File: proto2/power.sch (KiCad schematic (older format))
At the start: 2 parts, among them U13 AP1117-50, U14 JTD1548S15

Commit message: Routed Board.
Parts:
- removed U14: JTD1548S15, Converter_DCDC:Converter_DCDC_XP_POWER_JTDxxxxxxx_THT, symbol Converter_DCDC:JTD1548S15
- added C43, C49: 1nF 2kV, Capacitor_SMD:C_0805_2012Metric, symbol Device:C_Small
- added C44, C47: 330uF, Capacitor_SMD:C_0805_2012Metric, symbol Device:CP1_Small
- added C45, C46: 4.7uF, Capacitor_SMD:C_0805_2012Metric, symbol Device:C_Small
- added C48: 100uF, Capacitor_SMD:C_0805_2012Metric, symbol Device:C_Small
- added C50: 0.33uF, Capacitor_SMD:C_0805_2012Metric, symbol Device:C_Small
- added C51: 01.uF, Capacitor_SMD:C_0805_2012Metric, symbol Device:C_Small
- added C52, C53: 0.1uF, Capacitor_SMD:C_1206_3216Metric, symbol Device:C_Small
- added F13: 1A, Resistor_SMD:R_1206_3216Metric, symbol Device:Polyfuse_Small
- added F14, F15, F16, F17: 500mA, Resistor_SMD:R_0805_2012Metric, symbol Device:Polyfuse_Small
- added L43: 2.2uH, Inductor_BCR:Murata_LQH32PN2R2NN0L, symbol Device:L_Core_Ferrite_Small
- added PS1: CUI PDQE20, Converter_BCR:CUI_PDQE20, symbol BCR:CUI_PDQE20_ISOLATED_DCDC
- added R17, R18: 0R, Resistor_SMD:R_0805_2012Metric, symbol Device:R_Small
- added R19: R Trim Up, Capacitor_SMD:C_0805_2012Metric, symbol Device:R_Small
- added R20: R Trim Down, Capacitor_SMD:C_0805_2012Metric, symbol Device:R_Small
- added R21: 0R, Capacitor_SMD:C_1206_3216Metric, symbol Device:R_Small
- U13: value AP1117-50 -> LDO
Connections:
- net labels added: 5V_1, 5V_2, 5V_3, 5V_4, GNDPWR, TRIM, VIN
- wire segments 15 -> 93
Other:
- note added: "DNP:\nC50\nC51\nU13"
- note added: "DNP:\nC52\nC53\nR18"
- note added: "DNP:\nR19\nR20"
- note added: "https://electronics.stackexchange.com/questions/19561/should-chassis-ground-be-attached-to-digital-ground"
- moved on the sheet: U13

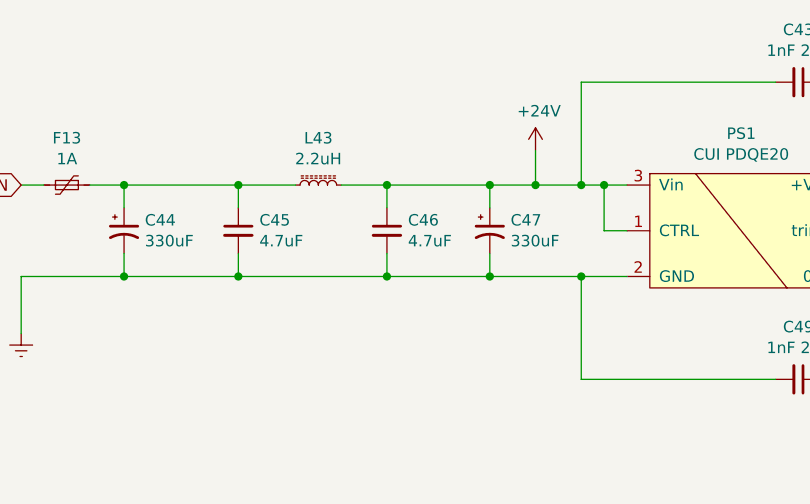
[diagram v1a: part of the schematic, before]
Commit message: Added correct cap and moved DIP switches.
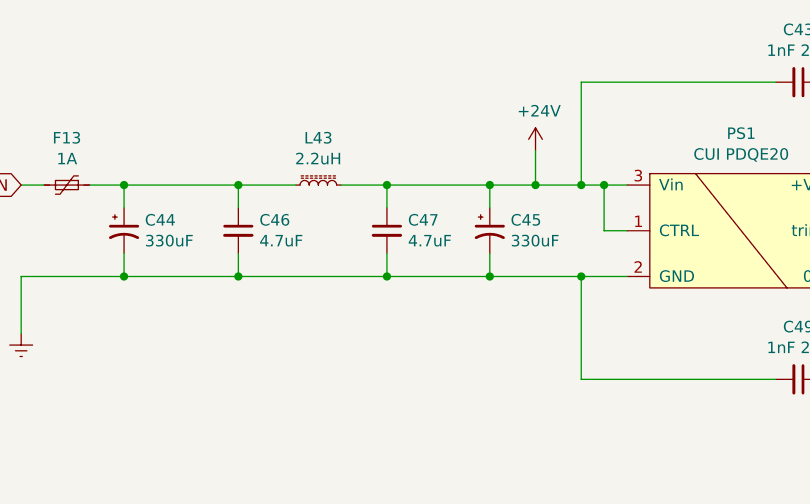
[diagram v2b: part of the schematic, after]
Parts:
- C44: footprint Capacitor_SMD:C_0805_2012Metric -> Capacitor_BCR:CP_Elec_13x12.5
- C45: renamed from C47; footprint Capacitor_SMD:C_0805_2012Metric -> Capacitor_BCR:CP_Elec_13x12.5
- U13: footprint Package_TO_SOT_SMD:SOT-223-3_TabPin2 -> JLCPCB:TO-252-2
- renumbered C45 to C46, C46 to C47
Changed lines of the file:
@@
 F 0 "U13" H 3900 5742 50  0000 C CNN
 F 1 "LDO" H 3900 5651 50  0000 C CNN
-F 2 "Package_TO_SOT_SMD:SOT-223-3_TabPin2" H 3900 5700 50  0001 C CNN
+F 2 "JLCPCB:TO-252-2" H 3900 5700 50  0001 C CNN
 F 3 "http://www.diodes.com/datasheets/AP1117.pdf" H 4000 5250 50  0001 C CNN
 	1    3900 5500
@@
 F 0 "C44" H 1441 2046 50  0000 L CNN
 F 1 "330uF" H 1441 1955 50  0000 L CNN
-F 2 "Capacitor_SMD:C_0805_2012Metric" H 1350 2000 50  0001 C CNN
+F 2 "Capacitor_BCR:CP_Elec_13x12.5" H 1350 2000 50  0001 C CNN
 F 3 "~" H 1350 2000 50  0001 C CNN
 	1    1350 2000
@@
 $EndComp
 $Comp
-L Device:CP1_Small C47
+L Device:CP1_Small C45
 U 1 1 61BAC8B9
 P 2950 2000
-F 0 "C47" H 3041 2046 50  0000 L CNN
+F 0 "C45" H 3041 2046 50  0000 L CNN
 F 1 "330uF" H 3041 1955 50  0000 L CNN
-F 2 "Capacitor_SMD:C_0805_2012Metric" H 2950 2000 50  0001 C CNN
+F 2 "Capacitor_BCR:CP_Elec_13x12.5" H 2950 2000 50  0001 C CNN
 F 3 "~" H 2950 2000 50  0001 C CNN
 	1    2950 2000
@@
 $EndComp
 $Comp
-L Device:C_Small C46
+L Device:C_Small C47
 U 1 1 61BB6AD1
 P 2500 2000
-F 0 "C46" H 2592 2046 50  0000 L CNN
+F 0 "C47" H 2592 2046 50  0000 L CNN
 F 1 "4.7uF" H 2592 1955 50  0000 L CNN
 F 2 "Capacitor_SMD:C_0805_2012Metric" H 2500 2000 50  0001 C CNN
@@
 $EndComp
 $Comp
-L Device:C_Small C45
+L Device:C_Small C46
 U 1 1 61BB959C
 P 1850 2000
-F 0 "C45" H 1942 2046 50  0000 L CNN
+F 0 "C46" H 1942 2046 50  0000 L CNN
 F 1 "4.7uF" H 1942 1955 50  0000 L CNN
 F 2 "Capacitor_SMD:C_0805_2012Metric" H 1850 2000 50  0001 C CNN

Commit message: Finished routing board and other changes, bad commit message, I know.
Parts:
- C43, C49: footprint Capacitor_SMD:C_0805_2012Metric -> Capacitor_SMD:C_1206_3216Metric; LCSC (none) -> C9196
- C44, C45: LCSC (none) -> C94443
- C46, C47: footprint Capacitor_SMD:C_0805_2012Metric -> Capacitor_SMD:C_1206_3216Metric; LCSC (none) -> C29823
- C48: footprint Capacitor_SMD:C_0805_2012Metric -> Capacitor_SMD:C_1206_3216Metric; LCSC (none) -> C312983
- C50: LCSC (none) -> C1740
- C51: value 01.uF -> 0.1uF; LCSC (none) -> C49678
- C52, C53: footprint Capacitor_SMD:C_1206_3216Metric -> Capacitor_SMD:C_0805_2012Metric; LCSC (none) -> C49678
- F13: LCSC (none) -> C70077
- F14, F15, F16, F17: LCSC (none) -> C70057
- L43: value 2.2uH -> 2.2uH 1.6A; LCSC (none) -> C86074; Manufacturer (none) -> Murata; Part Number (none) -> LQH32PN2R2NN0L
- PS1: Manufacturer (none) -> CUI; Part Number (none) -> PDQE20
- R17, R18: LCSC (none) -> C17477
- R21: LCSC (none) -> C17888
- U13: LCSC (none) -> C58069
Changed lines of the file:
@@
 F 2 "JLCPCB:TO-252-2" H 3900 5700 50  0001 C CNN
 F 3 "http://www.diodes.com/datasheets/AP1117.pdf" H 4000 5250 50  0001 C CNN
+F 4 "C58069" H 3900 5500 50  0001 C CNN "LCSC"
 	1    3900 5500
 	1    0    0    -1
@@
 F 2 "Converter_BCR:CUI_PDQE20" H 3750 2000 50  0001 C CNN
 F 3 "" H 3750 2000 50  0001 C CNN
+F 4 "CUI" H 4050 2000 50  0001 C CNN "Manufacturer"
+F 5 "PDQE20" H 4050 2000 50  0001 C CNN "Part Number"
 	1    4050 2000
 	1    0    0    -1
@@
 P 2200 1800
 F 0 "L43" V 2405 1800 50  0000 C CNN
-F 1 "2.2uH" V 2314 1800 50  0000 C CNN
+F 1 "2.2uH 1.6A" V 2314 1800 50  0000 C CNN
 F 2 "Inductor_BCR:Murata_LQH32PN2R2NN0L" H 2200 1800 50  0001 C CNN
 F 3 "~" H 2200 1800 50  0001 C CNN
+F 4 "C86074" H 2200 1800 50  0001 C CNN "LCSC"
+F 5 "Murata" H 2200 1800 50  0001 C CNN "Manufacturer"
+F 6 "LQH32PN2R2NN0L" H 2200 1800 50  0001 C CNN "Part Number"
 	1    2200 1800
 	0    -1   -1   0
@@
 F 0 "C48" H 5242 2046 50  0000 L CNN
 F 1 "100uF" H 5242 1955 50  0000 L CNN
-F 2 "Capacitor_SMD:C_0805_2012Metric" H 5150 2000 50  0001 C CNN
+F 2 "Capacitor_SMD:C_1206_3216Metric" H 5150 2000 50  0001 C CNN
 F 3 "~" H 5150 2000 50  0001 C CNN
+F 4 "C312983" H 5150 2000 50  0001 C CNN "LCSC"
 	1    5150 2000
 	1    0    0    -1
@@
 F 0 "C43" V 4071 1350 50  0000 C CNN
 F 1 "1nF 2kV" V 4162 1350 50  0000 C CNN
-F 2 "Capacitor_SMD:C_0805_2012Metric" H 4300 1350 50  0001 C CNN
+F 2 "Capacitor_SMD:C_1206_3216Metric" H 4300 1350 50  0001 C CNN
 F 3 "~" H 4300 1350 50  0001 C CNN
+F 4 "C9196" H 4300 1350 50  0001 C CNN "LCSC"
 	1    4300 1350
 	0    1    1    0
@@
 F 0 "C49" V 4071 2650 50  0000 C CNN
 F 1 "1nF 2kV" V 4162 2650 50  0000 C CNN
-F 2 "Capacitor_SMD:C_0805_2012Metric" H 4300 2650 50  0001 C CNN
+F 2 "Capacitor_SMD:C_1206_3216Metric" H 4300 2650 50  0001 C CNN
 F 3 "~" H 4300 2650 50  0001 C CNN
+F 4 "C9196" H 4300 2650 50  0001 C CNN "LCSC"
 	1    4300 2650
 	0    1    1    0
@@
 F 2 "Capacitor_BCR:CP_Elec_13x12.5" H 1350 2000 50  0001 C CNN
 F 3 "~" H 1350 2000 50  0001 C CNN
+F 4 "C94443" H 1350 2000 50  0001 C CNN "LCSC"
 	1    1350 2000
 	1    0    0    -1
@@
 F 2 "Capacitor_BCR:CP_Elec_13x12.5" H 2950 2000 50  0001 C CNN
 F 3 "~" H 2950 2000 50  0001 C CNN
+F 4 "C94443" H 2950 2000 50  0001 C CNN "LCSC"
 	1    2950 2000
 	1    0    0    -1
@@
 F 0 "C47" H 2592 2046 50  0000 L CNN
 F 1 "4.7uF" H 2592 1955 50  0000 L CNN
-F 2 "Capacitor_SMD:C_0805_2012Metric" H 2500 2000 50  0001 C CNN
+F 2 "Capacitor_SMD:C_1206_3216Metric" H 2500 2000 50  0001 C CNN
 F 3 "~" H 2500 2000 50  0001 C CNN
+F 4 "C29823" H 2500 2000 50  0001 C CNN "LCSC"
 	1    2500 2000
 	1    0    0    -1
@@
 F 0 "C46" H 1942 2046 50  0000 L CNN
 F 1 "4.7uF" H 1942 1955 50  0000 L CNN
-F 2 "Capacitor_SMD:C_0805_2012Metric" H 1850 2000 50  0001 C CNN
+F 2 "Capacitor_SMD:C_1206_3216Metric" H 1850 2000 50  0001 C CNN
 F 3 "~" H 1850 2000 50  0001 C CNN
+F 4 "C29823" H 1850 2000 50  0001 C CNN "LCSC"
 	1    1850 2000
 	1    0    0    -1
@@
 F 2 "Capacitor_SMD:C_1206_3216Metric" H 3900 4900 50  0001 C CNN
 F 3 "~" H 3900 4900 50  0001 C CNN
+F 4 "C17888" H 3900 4900 50  0001 C CNN "LCSC"
 	1    3900 4900
 	0    1    1    0
@@
 F 2 "Capacitor_SMD:C_0805_2012Metric" H 3200 5800 50  0001 C CNN
 F 3 "~" H 3200 5800 50  0001 C CNN
+F 4 "C1740" H 3200 5800 50  0001 C CNN "LCSC"
 	1    3200 5800
 	1    0    0    -1
@@
 P 4600 5800
 F 0 "C51" H 4692 5846 50  0000 L CNN
-F 1 "01.uF" H 4692 5755 50  0000 L CNN
+F 1 "0.1uF" H 4692 5755 50  0000 L CNN
 F 2 "Capacitor_SMD:C_0805_2012Metric" H 4600 5800 50  0001 C CNN
 F 3 "~" H 4600 5800 50  0001 C CNN
+F 4 "C49678" H 4600 5800 50  0001 C CNN "LCSC"
 	1    4600 5800
 	1    0    0    -1
@@
 F 2 "Resistor_SMD:R_1206_3216Metric" H 1150 1600 50  0001 L CNN
 F 3 "~" H 1100 1800 50  0001 C CNN
+F 4 "C70077" H 1100 1800 50  0001 C CNN "LCSC"
 	1    1100 1800
 	0    1    1    0
@@
 F 2 "Resistor_SMD:R_0805_2012Metric" H 7000 5550 50  0001 L CNN
 F 3 "~" H 6950 5750 50  0001 C CNN
+F 4 "C70057" H 6950 5750 50  0001 C CNN "LCSC"
 	1    6950 5750
 	0    1    1    0
@@
 F 2 "Resistor_SMD:R_0805_2012Metric" H 7000 5250 50  0001 L CNN
 F 3 "~" H 6950 5450 50  0001 C CNN
+F 4 "C70057" H 6950 5450 50  0001 C CNN "LCSC"
 	1    6950 5450
 	0    1    1    0
@@
 F 2 "Resistor_SMD:R_0805_2012Metric" H 7000 4650 50  0001 L CNN
 F 3 "~" H 6950 4850 50  0001 C CNN
+F 4 "C70057" H 6950 4850 50  0001 C CNN "LCSC"
 	1    6950 4850
 	0    1    1    0
@@
 F 2 "Resistor_SMD:R_0805_2012Metric" H 7000 4950 50  0001 L CNN
 F 3 "~" H 6950 5150 50  0001 C CNN
+F 4 "C70057" H 6950 5150 50  0001 C CNN "LCSC"
 	1    6950 5150
 	0    1    1    0
@@
 F 2 "Resistor_SMD:R_0805_2012Metric" H 8750 4500 50  0001 C CNN
 F 3 "~" H 8750 4500 50  0001 C CNN
+F 4 "C17477" H 8750 4500 50  0001 C CNN "LCSC"
 	1    8750 4500
 	0    1    1    0
@@
 F 2 "Resistor_SMD:R_0805_2012Metric" H 9250 4500 50  0001 C CNN
 F 3 "~" H 9250 4500 50  0001 C CNN
+F 4 "C17477" H 9250 4500 50  0001 C CNN "LCSC"
 	1    9250 4500
 	0    1    1    0
@@
 F 0 "C52" V 8521 4850 50  0000 C CNN
 F 1 "0.1uF" V 8612 4850 50  0000 C CNN
-F 2 "Capacitor_SMD:C_1206_3216Metric" H 8750 4850 50  0001 C CNN
+F 2 "Capacitor_SMD:C_0805_2012Metric" H 8750 4850 50  0001 C CNN
 F 3 "~" H 8750 4850 50  0001 C CNN
+F 4 "C49678" H 8750 4850 50  0001 C CNN "LCSC"
 	1    8750 4850
 	0    1    1    0
@@
 F 0 "C53" V 9021 4850 50  0000 C CNN
 F 1 "0.1uF" V 9112 4850 50  0000 C CNN
-F 2 "Capacitor_SMD:C_1206_3216Metric" H 9250 4850 50  0001 C CNN
+F 2 "Capacitor_SMD:C_0805_2012Metric" H 9250 4850 50  0001 C CNN
 F 3 "~" H 9250 4850 50  0001 C CNN
+F 4 "C49678" H 9250 4850 50  0001 C CNN "LCSC"
 	1    9250 4850
 	0    1    1    0

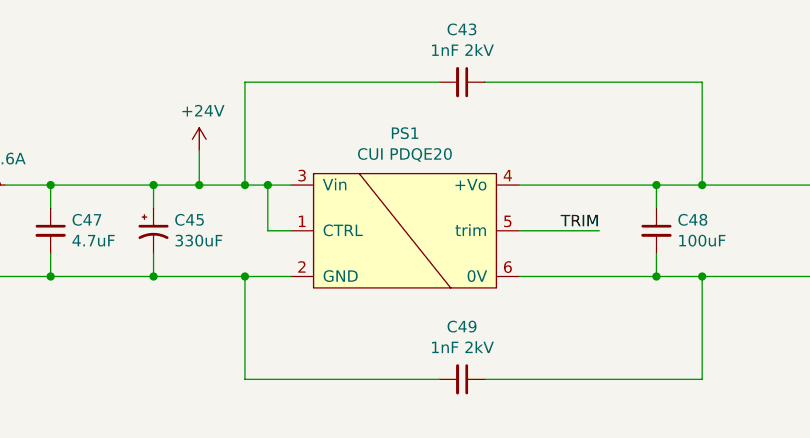
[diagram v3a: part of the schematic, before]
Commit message: Updated filters and Power supply foorptint.
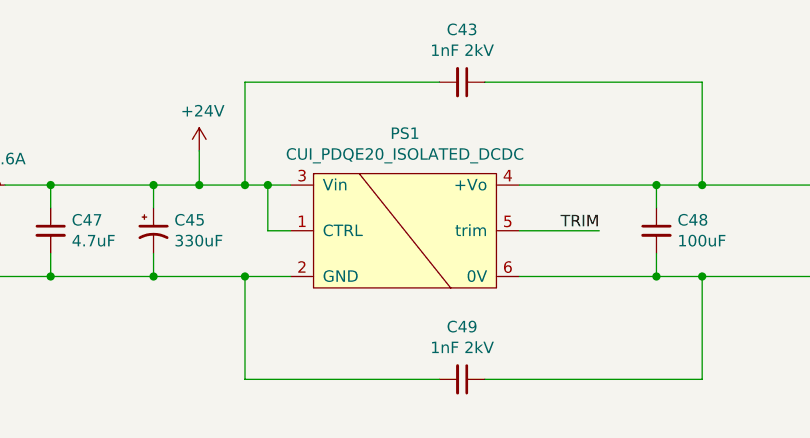
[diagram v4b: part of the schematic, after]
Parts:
- PS1: value CUI PDQE20 -> CUI_PDQE20_ISOLATED_DCDC; Manufacturer CUI -> (none); Part Number PDQE20 -> (none)
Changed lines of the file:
@@
-$EndComp
-$Comp
-L BCR:CUI_PDQE20_ISOLATED_DCDC PS1
-U 1 1 61B90860
-P 4050 2000
-F 0 "PS1" H 4050 2425 50  0000 C CNN
-F 1 "CUI PDQE20" H 4050 2334 50  0000 C CNN
-F 2 "Converter_BCR:CUI_PDQE20" H 3750 2000 50  0001 C CNN
-F 3 "" H 3750 2000 50  0001 C CNN
-F 4 "CUI" H 4050 2000 50  0001 C CNN "Manufacturer"
-F 5 "PDQE20" H 4050 2000 50  0001 C CNN "Part Number"
-	1    4050 2000
-	1    0    0    -1
 $EndComp
 $Comp
@@
 	1    0    0    -1
 $EndComp
+$Comp
+L BCR:CUI_PDQE20_ISOLATED_DCDC PS1
+U 1 1 61BF7DE1
+P 4050 2000
+F 0 "PS1" H 4050 2425 50  0000 C CNN
+F 1 "CUI_PDQE20_ISOLATED_DCDC" H 4050 2334 50  0000 C CNN
+F 2 "Converter_BCR:CUI_PDQE20" H 3750 2000 50  0001 C CNN
+F 3 "" H 3750 2000 50  0001 C CNN
+	1    4050 2000
+	1    0    0    -1
+$EndComp
